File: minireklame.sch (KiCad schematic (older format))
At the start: 54 parts, among them IC1 ATXMEGA64A4U-A, P1 CONN_01X04, P10 CONN_01X04, P11 CONN_01X04, P12 CONN_01X04, P13 CONN_01X04, P14 CONN_01X04, P15 CONN_01X04, P16 CONN_01X04, P17 Screw_Terminal_1x02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

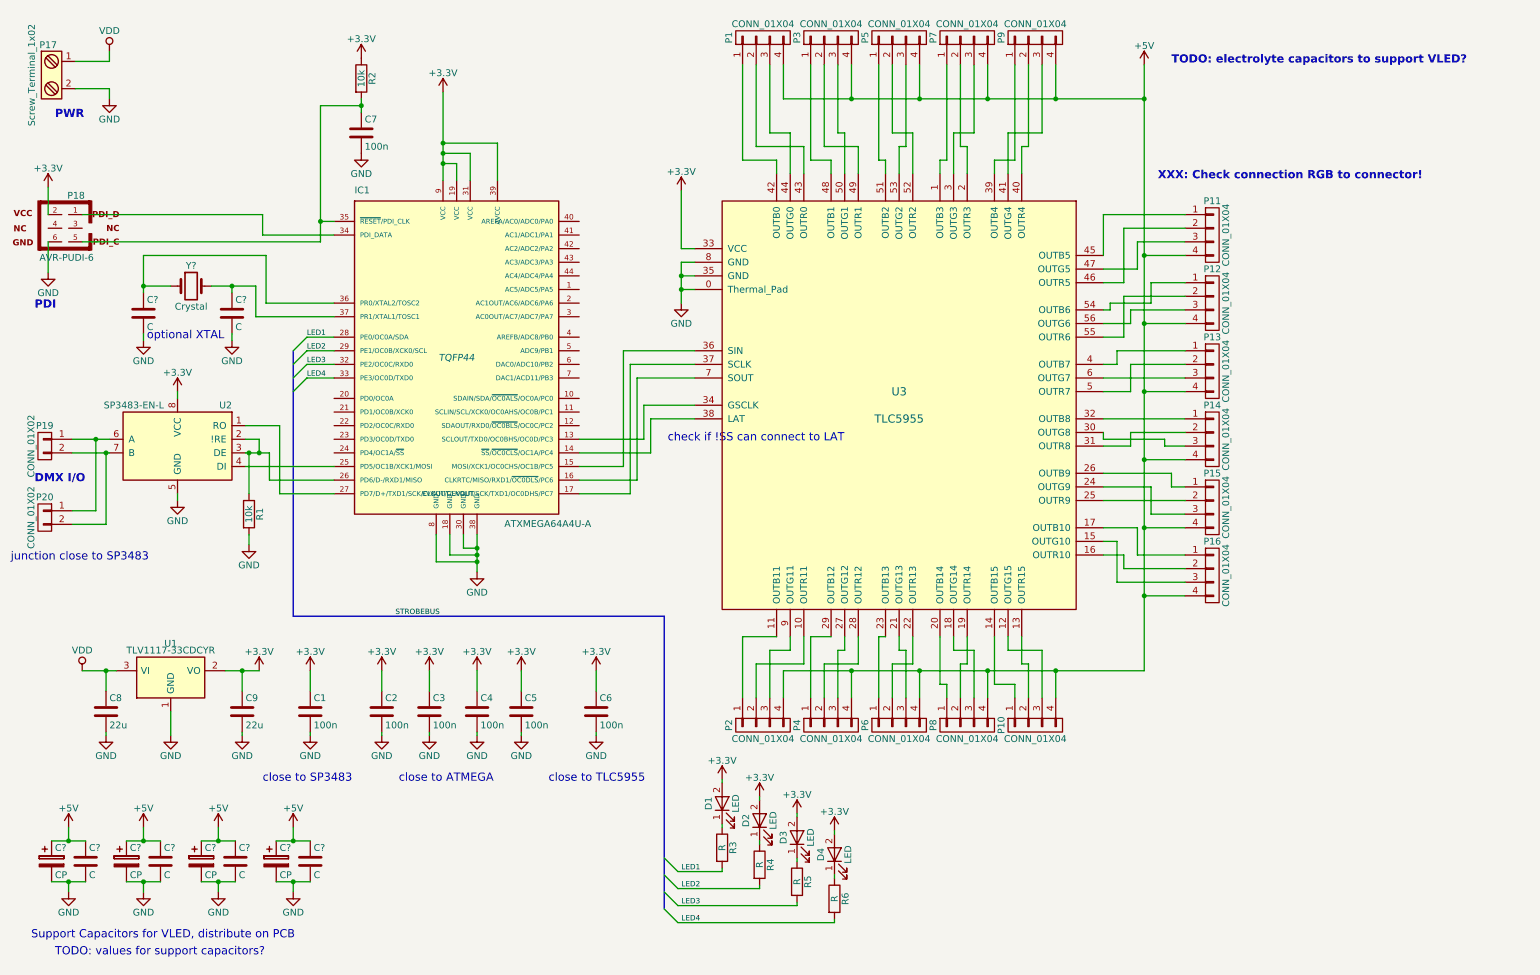
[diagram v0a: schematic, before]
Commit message: rearranging pin positions of TLC5955 so simplify schematic
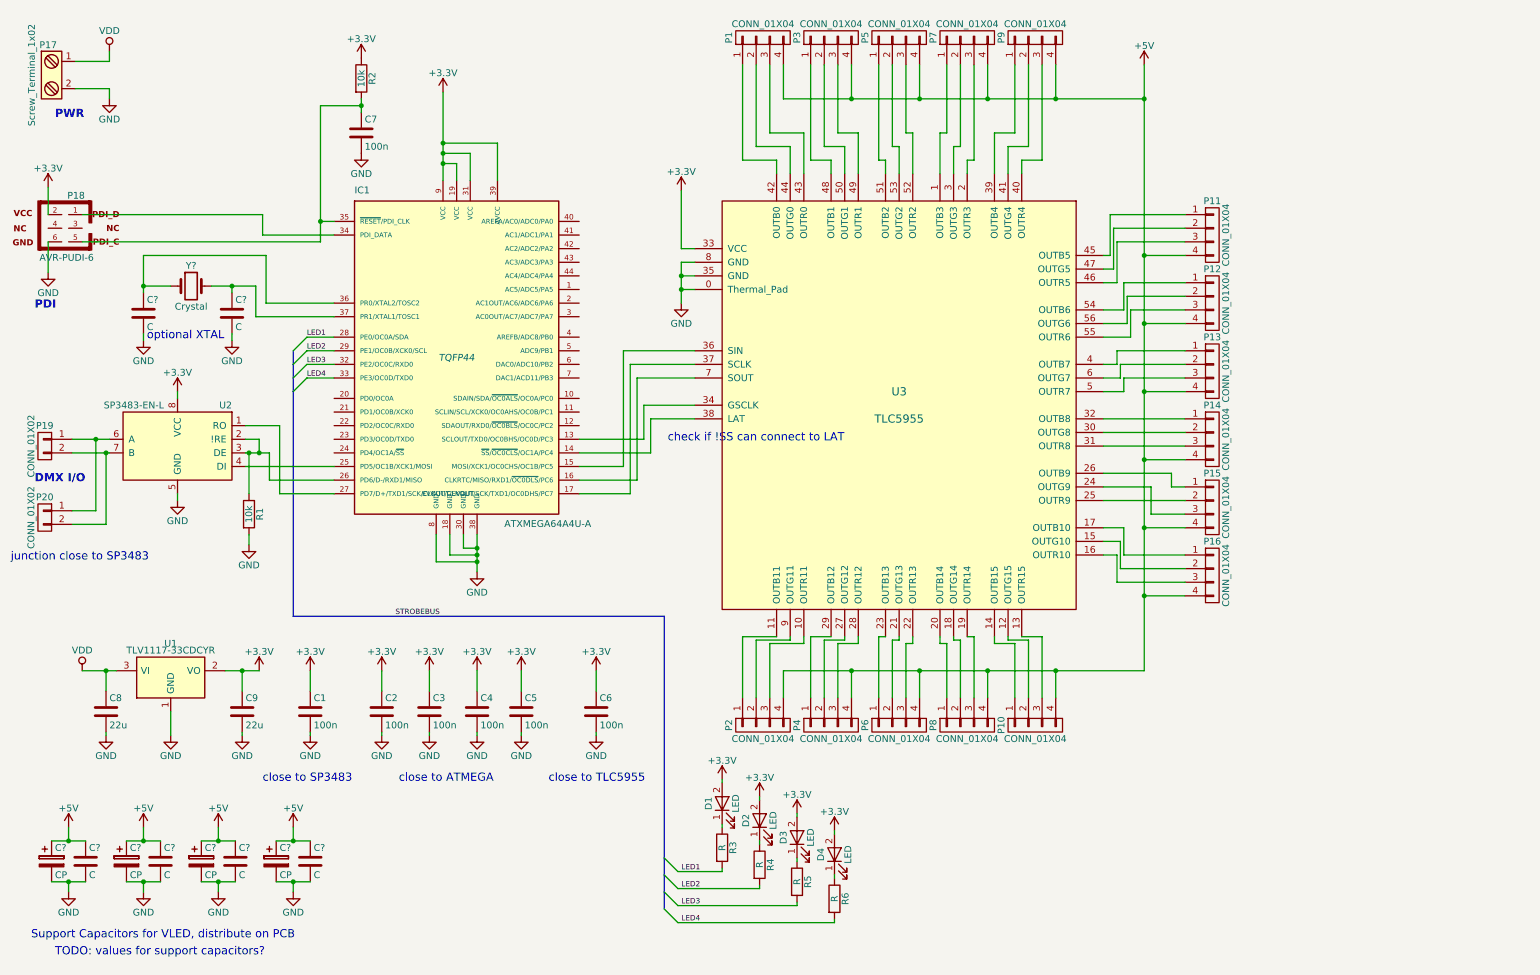
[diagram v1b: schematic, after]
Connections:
- net at U3.10 (OUTR11): now also P2.3 (P3); no longer P2.2 (P2)
- net at U3.12 (OUTG15): now also P10.2 (P2); no longer P10.3 (P3)
- net at U3.13 (OUTR15): now also P10.3 (P3); no longer P10.2 (P2)
- net at U3.15 (OUTG10): now also P16.2 (P2); no longer P16.3 (P3)
- net at U3.16 (OUTR10): now also P16.3 (P3); no longer P16.2 (P2)
- net at U3.18 (OUTG14): now also P8.2 (P2); no longer P8.3 (P3)
- net at U3.19 (OUTR14): now also P8.3 (P3); no longer P8.2 (P2)
- net at U3.2 (OUTR3): now also P7.3 (P3); no longer P7.2 (P2)
- net at U3.21 (OUTG13): now also P6.2 (P2); no longer P6.3 (P3)
- net at U3.22 (OUTR13): now also P6.3 (P3); no longer P6.2 (P2)
- net at U3.27 (OUTG12): now also P4.2 (P2); no longer P4.3 (P3)
- net at U3.28 (OUTR12): now also P4.3 (P3); no longer P4.2 (P2)
- net at U3.3 (OUTG3): now also P7.2 (P2); no longer P7.3 (P3)
- net at U3.30 (OUTG8): now also P14.2 (P2); no longer P14.3 (P3)
- net at U3.31 (OUTR8): now also P14.3 (P3); no longer P14.2 (P2)
- net at U3.40 (OUTR4): now also P9.3 (P3); no longer P9.2 (P2)
- net at U3.41 (OUTG4): now also P9.2 (P2); no longer P9.3 (P3)
- net at U3.43 (OUTR0): now also P1.3 (P3); no longer P1.2 (P2)
- net at U3.44 (OUTG0): now also P1.2 (P2); no longer P1.3 (P3)
- net at U3.46 (OUTR5): now also P11.3 (P3); no longer P11.2 (P2)
- net at U3.47 (OUTG5): now also P11.2 (P2); no longer P11.3 (P3)
- net at U3.49 (OUTR1): now also P3.3 (P3); no longer P3.2 (P2)
- net at U3.5 (OUTR7): now also P13.3 (P3); no longer P13.2 (P2)
- net at U3.50 (OUTG1): now also P3.2 (P2); no longer P3.3 (P3)
- net at U3.52 (OUTR2): now also P5.3 (P3); no longer P5.2 (P2)
- net at U3.53 (OUTG2): now also P5.2 (P2); no longer P5.3 (P3)
- net at U3.55 (OUTR6): now also P12.3 (P3); no longer P12.2 (P2)
- net at U3.56 (OUTG6): now also P12.2 (P2); no longer P12.3 (P3)
- net at U3.6 (OUTG7): now also P13.2 (P2); no longer P13.3 (P3)
- net at U3.9 (OUTG11): now also P2.2 (P2); no longer P2.3 (P3)
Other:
- note removed: "TODO: electrolyte capacitors to support VLED?"
- note removed: "XXX: Check connection RGB to connector!"

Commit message: annotating component IDs
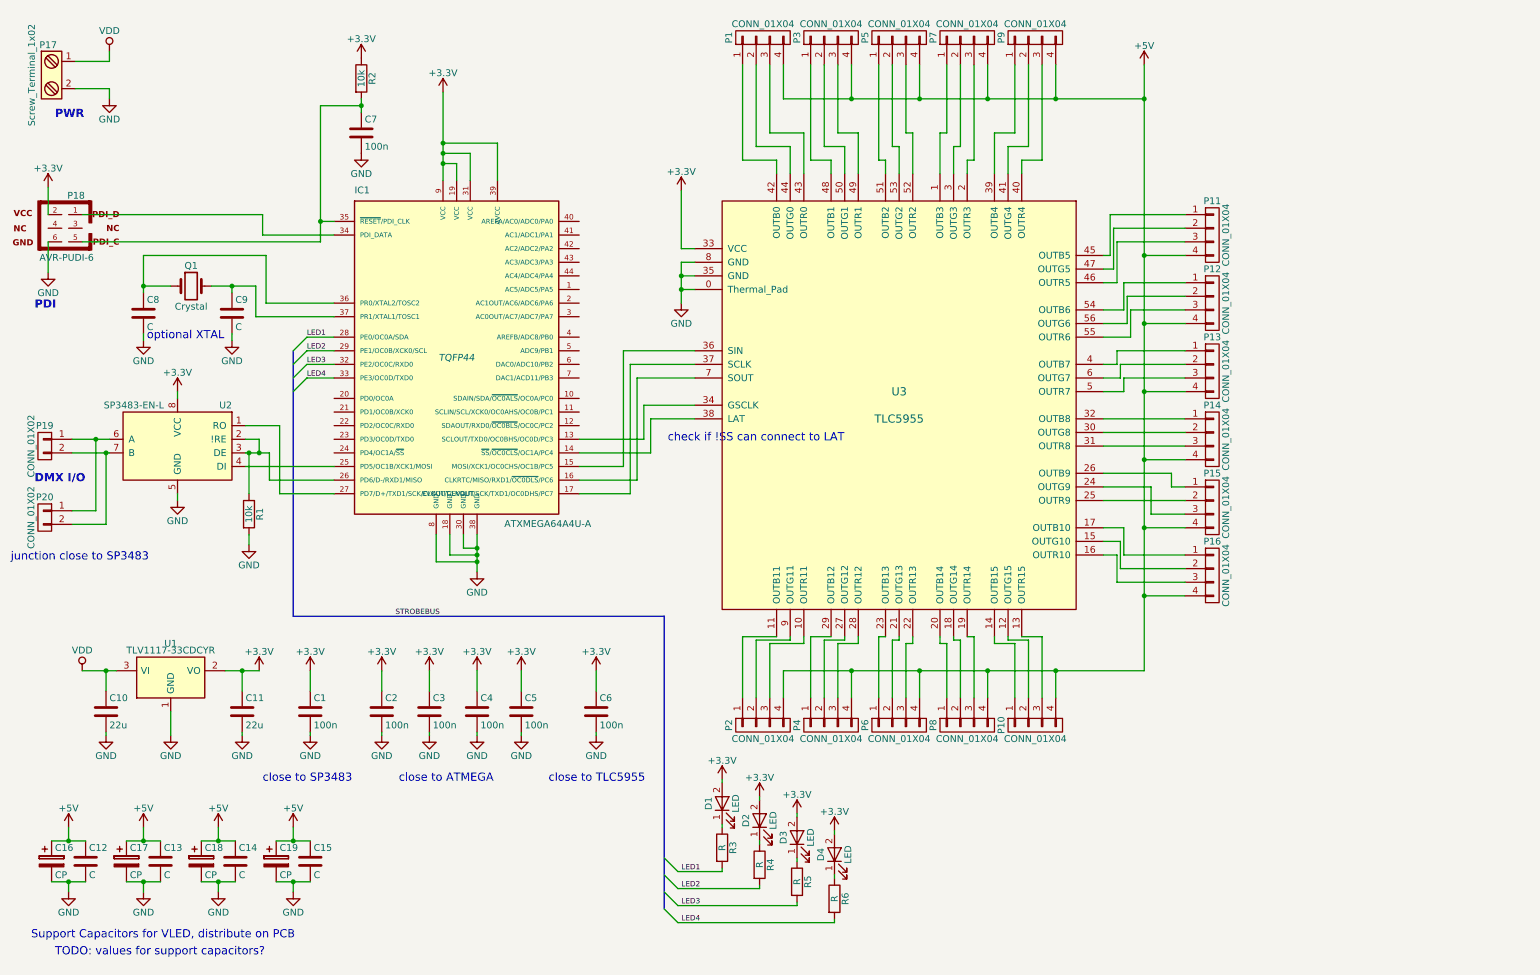
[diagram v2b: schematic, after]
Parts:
- gave numbers to parts that had none: 11
- renumbered C8 to C10, C9 to C11

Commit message: exchanging GSCLK and LAT connection
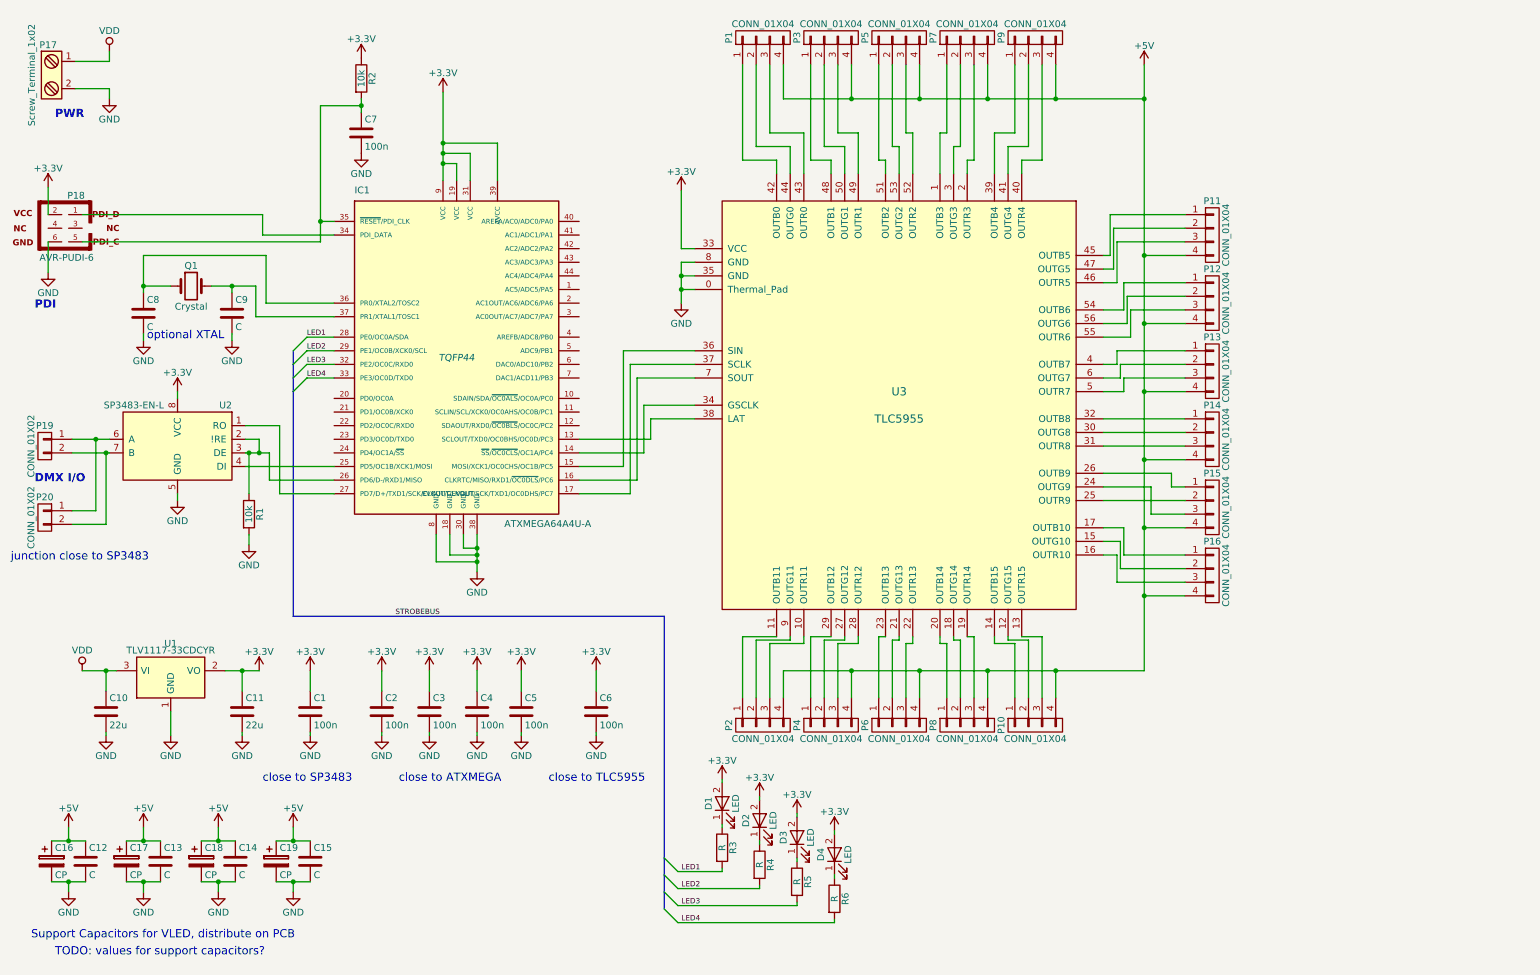
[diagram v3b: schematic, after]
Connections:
- net at U3.34 (GSCLK): now also IC1.14 (~SS~/~OC0CLS~/OC1A/PC4); no longer IC1.13 (SCLOUT/TXD0/OC0BHS/OC0D/PC3)
- net at U3.38 (LAT): now also IC1.13 (SCLOUT/TXD0/OC0BHS/OC0D/PC3); no longer IC1.14 (~SS~/~OC0CLS~/OC1A/PC4)
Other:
- note added: "close to ATXMEGA"
- note removed: "check if !SS can connect to LAT"
- note removed: "close to ATMEGA"
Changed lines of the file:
@@
 $EndComp
 Wire Wire Line
-	1025 3900 1300 3900
-Wire Wire Line
-	1025 4000 1300 4000
+	1025 3900 1200 3900
+Wire Wire Line
+	1200 3900 1300 3900
+Wire Wire Line
+	1025 4000 1275 4000
+Wire Wire Line
+	1275 4000 1300 4000
 Wire Wire Line
 	1800 3550 1800 3600
@@
 	3700 4600 3700 4800
 Wire Wire Line
-	4000 4600 4000 4875
+	4000 4600 4000 4700
+Wire Wire Line
+	4000 4700 4000 4750
+Wire Wire Line
+	4000 4750 4000 4800
+Wire Wire Line
+	4000 4800 4000 4875
 Wire Wire Line
 	3900 4600 3900 4700
@@
 	5500 2800 5600 2800
 Wire Wire Line
-	5500 2600 5500 2900
+	5500 2600 5500 2700
+Wire Wire Line
+	5500 2700 5500 2800
+Wire Wire Line
+	5500 2800 5500 2900
 Wire Wire Line
 	5600 2700 5500 2700
@@
 Connection ~ 5500 2700
 Wire Wire Line
-	3750 1350 3750 2000
+	3750 1350 3750 1725
+Wire Wire Line
+	3750 1725 3750 1800
+Wire Wire Line
+	3750 1800 3750 1875
+Wire Wire Line
+	3750 1875 3750 2000
 Wire Wire Line
 	5500 2500 5600 2500
@@
 	2300 4100 2950 4100
 Wire Wire Line
-	2300 4000 2475 4000
+	2300 4000 2325 4000
+Wire Wire Line
+	2325 4000 2400 4000
+Wire Wire Line
+	2400 4000 2475 4000
 Wire Wire Line
 	2475 4000 2475 4200
@@
 	6250 1150 6250 1400
 Wire Wire Line
-	6250 1400 8900 1400
-Wire Wire Line
-	8900 5600 8900 1150
+	6250 1400 6750 1400
+Wire Wire Line
+	6750 1400 7250 1400
+Wire Wire Line
+	7250 1400 7750 1400
+Wire Wire Line
+	7750 1400 8250 1400
+Wire Wire Line
+	8250 1400 8900 1400
+Wire Wire Line
+	8900 5600 8900 5050
+Wire Wire Line
+	8900 5050 8900 4550
+Wire Wire Line
+	8900 4550 8900 4050
+Wire Wire Line
+	8900 4050 8900 3550
+Wire Wire Line
+	8900 3550 8900 3050
+Wire Wire Line
+	8900 3050 8900 2550
+Wire Wire Line
+	8900 2550 8900 1400
+Wire Wire Line
+	8900 1400 8900 1150
 Wire Wire Line
 	6750 1150 6750 1400
@@
 	6250 5800 6250 5600
 Wire Wire Line
-	6250 5600 8900 5600
+	6250 5600 6750 5600
+Wire Wire Line
+	6750 5600 7250 5600
+Wire Wire Line
+	7250 5600 7750 5600
+Wire Wire Line
+	7750 5600 8250 5600
+Wire Wire Line
+	8250 5600 8900 5600
 Connection ~ 8900 5050
 Wire Wire Line
@@
 $EndComp
 Wire Wire Line
-	1100 5600 1350 5600
+	1100 5600 1275 5600
+Wire Wire Line
+	1275 5600 1350 5600
 $Comp
 L GND #PWR09
@@
 	2850 1450 3150 1450
 Wire Wire Line
-	3150 1400 3150 1500
+	3150 1400 3150 1450
+Wire Wire Line
+	3150 1450 3150 1500
 Connection ~ 3150 1450
 $Comp
@@
 	1050 1325 1300 1325
 Wire Wire Line
-	2850 1450 2850 2450
+	2850 1450 2850 2300
+Wire Wire Line
+	2850 2300 2850 2450
 Text Notes 900  1550 0    60   ~ 12
 PWR
@@
 	1750 5900 1750 6075
 Wire Wire Line
-	2150 5600 2400 5600
+	2150 5600 2275 5600
+Wire Wire Line
+	2275 5600 2400 5600
 Wire Wire Line
 	2275 5750 2275 5600
@@
 	4325 5750 4325 5600
 Text Notes 3425 6425 0    60   ~ 0
-close to ATMEGA
+close to ATXMEGA
 $Comp
 L +3.3V #PWR027
@@
 	5125 3350 5600 3350
 Wire Wire Line
-	4750 4000 5275 4000
-Wire Wire Line
-	5275 4000 5275 3750
-Wire Wire Line
 	5275 3750 5600 3750
 Wire Wire Line
-	4750 3900 5225 3900
-Wire Wire Line
-	5225 3900 5225 3650
-Wire Wire Line
 	5225 3650 5600 3650
-Text Notes 5400 3925 0    60   ~ 0
-check if !SS can connect to LAT
 $Comp
 L Crystal Q1
@@
 $EndComp
 Wire Wire Line
-	1550 2550 1550 2825
+	1550 2550 1550 2775
+Wire Wire Line
+	1550 2775 1550 2825
 Wire Wire Line
 	1550 2775 1750 2775
@@
 	2375 2775 2375 3000
 Wire Wire Line
-	2050 2775 2375 2775
+	2050 2775 2200 2775
+Wire Wire Line
+	2200 2775 2375 2775
 $Comp
 L C C8
@@
 $EndComp
 Wire Wire Line
-	1425 6850 1675 6850
+	1425 6850 1550 6850
+Wire Wire Line
+	1550 6850 1675 6850
 Wire Wire Line
 	1550 6750 1550 6850
 Connection ~ 1550 6850
 Wire Wire Line
-	1425 7150 1675 7150
+	1425 7150 1550 7150
+Wire Wire Line
+	1550 7150 1675 7150
 $Comp
 L GND #PWR035
@@
 $EndComp
 Wire Wire Line
-	1975 6850 2225 6850
+	1975 6850 2100 6850
+Wire Wire Line
+	2100 6850 2225 6850
 Wire Wire Line
 	2100 6750 2100 6850
 Connection ~ 2100 6850
 Wire Wire Line
-	1975 7150 2225 7150
+	1975 7150 2100 7150
+Wire Wire Line
+	2100 7150 2225 7150
 $Comp
 L GND #PWR037
@@
 $EndComp
 Wire Wire Line
-	875  6850 1125 6850
+	875  6850 1000 6850
+Wire Wire Line
+	1000 6850 1125 6850
 Wire Wire Line
 	1000 6750 1000 6850
 Connection ~ 1000 6850
 Wire Wire Line
-	875  7150 1125 7150
+	875  7150 1000 7150
+Wire Wire Line
+	1000 7150 1125 7150
 $Comp
 L GND #PWR039
@@
 $EndComp
 Wire Wire Line
-	2525 6850 2775 6850
+	2525 6850 2650 6850
+Wire Wire Line
+	2650 6850 2775 6850
 Wire Wire Line
 	2650 6750 2650 6850
 Connection ~ 2650 6850
 Wire Wire Line
-	2525 7150 2775 7150
+	2525 7150 2650 7150
+Wire Wire Line
+	2650 7150 2775 7150
 $Comp
 L GND #PWR041
@@
 	2750 3450 2650 3550
 Wire Bus Line
-	2650 3250 2650 5200
+	2650 3250 2650 3350
+Wire Bus Line
+	2650 3350 2650 3450
+Wire Bus Line
+	2650 3450 2650 3550
+Wire Bus Line
+	2650 3550 2650 5200
 Wire Bus Line
 	2650 5200 5375 5200
@@
 LED4
 Wire Bus Line
-	5375 5200 5375 7350
+	5375 5200 5375 6975
+Wire Bus Line
+	5375 6975 5375 7100
+Wire Bus Line
+	5375 7100 5375 7225
+Wire Bus Line
+	5375 7225 5375 7350
 Text Label 3400 5200 0    39   ~ 0
 STROBEBUS
@@
 Wire Wire Line
 	8050 5375 8050 5800
+Wire Wire Line
+	5275 3750 5275 3900
+Wire Wire Line
+	5275 3900 4750 3900
+Wire Wire Line
+	5225 3650 5225 4000
+Wire Wire Line
+	5225 4000 4750 4000
 $EndSCHEMATC
